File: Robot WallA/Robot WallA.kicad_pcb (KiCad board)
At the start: 4 copper layers, 170 x 100 mm, 316 parts, among them IC1 STM32F407IGT6, IC2 DS04-254-2-04BK-SMT, IC3 USBLC6-4SC6, IC4 USBLC6-4SC6, IC6 TLV75533PDBVR, IC7 ABXS005A4X341-SRZ, IC8 DRV8262DDVR, IC9 74LVC2G241DP-Q100H, J1 Conn_02x05_Female, J10 Conn_01x02, J11 Conn_01x02, J12 Conn_01x02, J13 10129383-916001ALF, J15 39501-1002, J16 39501-1002, J17 39501-1004, J18 39501-1004, J19 22-03-5035, J2 USB4216-03-A, J20 22-03-5035, J21 22-03-5035, J22 22-03-5035, J23 Conn_01x03, J24 281695-3, J25 Conn_01x03, J26 281695-3, J27 Conn_01x03, J28 281695-3, J29 Conn_01x03, J3 SS-90000-009, J30 39501-1002, J31 39501-1002, J32 Conn_01x03, J33 281695-3, J34 Conn_01x03, J35 SM04B-SRSS-TB, J36 SM04B-SRSS-TB, J37 SM04B-SRSS-TB, J38 SM02B-SRSS-TB_LF__SN_, J39 Conn_01x03, J4 USB_B_Micro, J40 SM03B-SRSS-TB_LF__SN_, J41 SM03B-SRSS-TB_LF__SN_, J42 SM03B-SRSS-TB_LF__SN_, J43 SM03B-SRSS-TB_LF__SN_, J44 SM02B-SRSS-TB_LF__SN_, J45 SM04B-SRSS-TB, J46 SM02B-SRSS-TB_LF__SN_, J47 SM02B-SRSS-TB_LF__SN_, J6 10129383-916001ALF, J7 Conn_01x02, J8 XT90PW_M, J9 Conn_01x02, Q1 BSS138, Q2 BSS138, Q3 BSS138, Q4 BSS119, Q5 BSS119, Q6 BSS138, SW1 Switch, T1 H1102NL, U1 FT231XS, U10 PTN78060W_EUW-7, U2 125700D00000G, U3 125700D00000G, U4 125700D00000G, U5 125700D00000G, U6 L298N, U7 LAN8742A, U8 PTN78020W, U9 PTN78060W_EUW-7, Y1 Crystal_GND24, Y2 Crystal_GND24

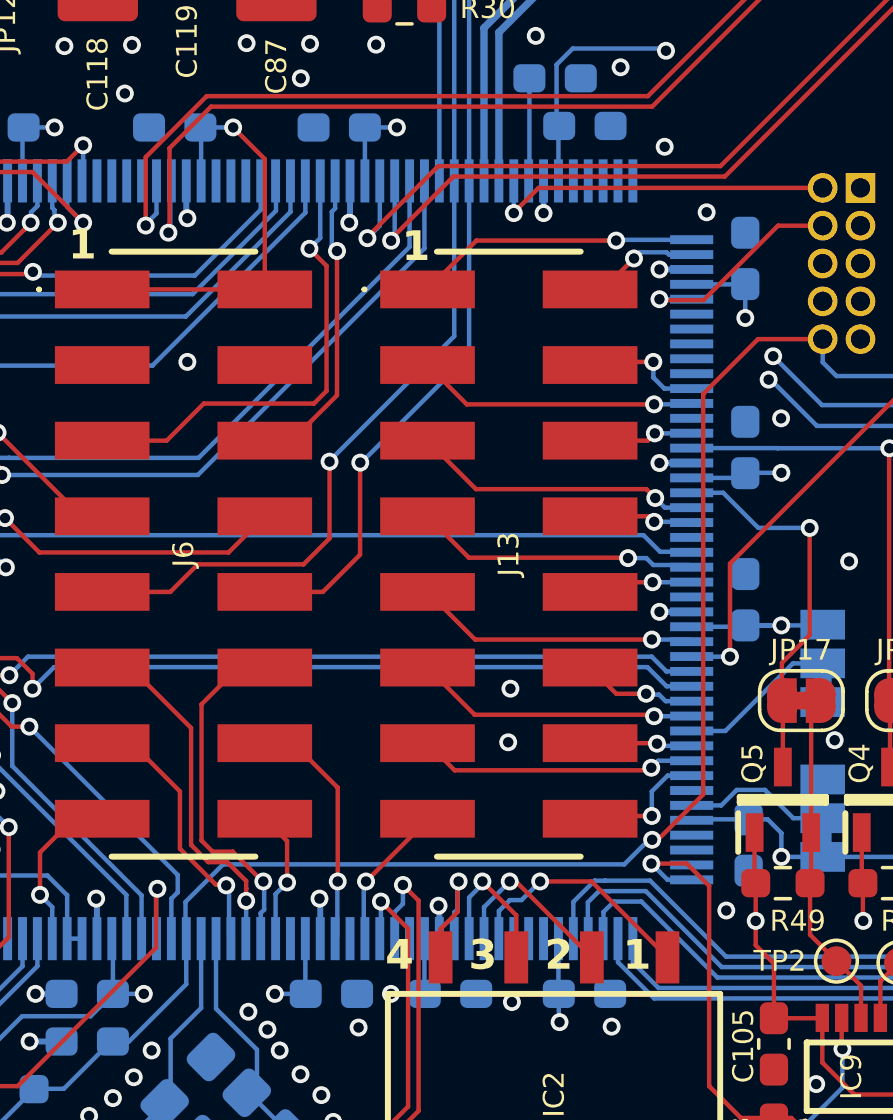
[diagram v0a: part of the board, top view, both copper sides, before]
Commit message: Modified a bit pin header pins to allow I2C,SPI and CAN
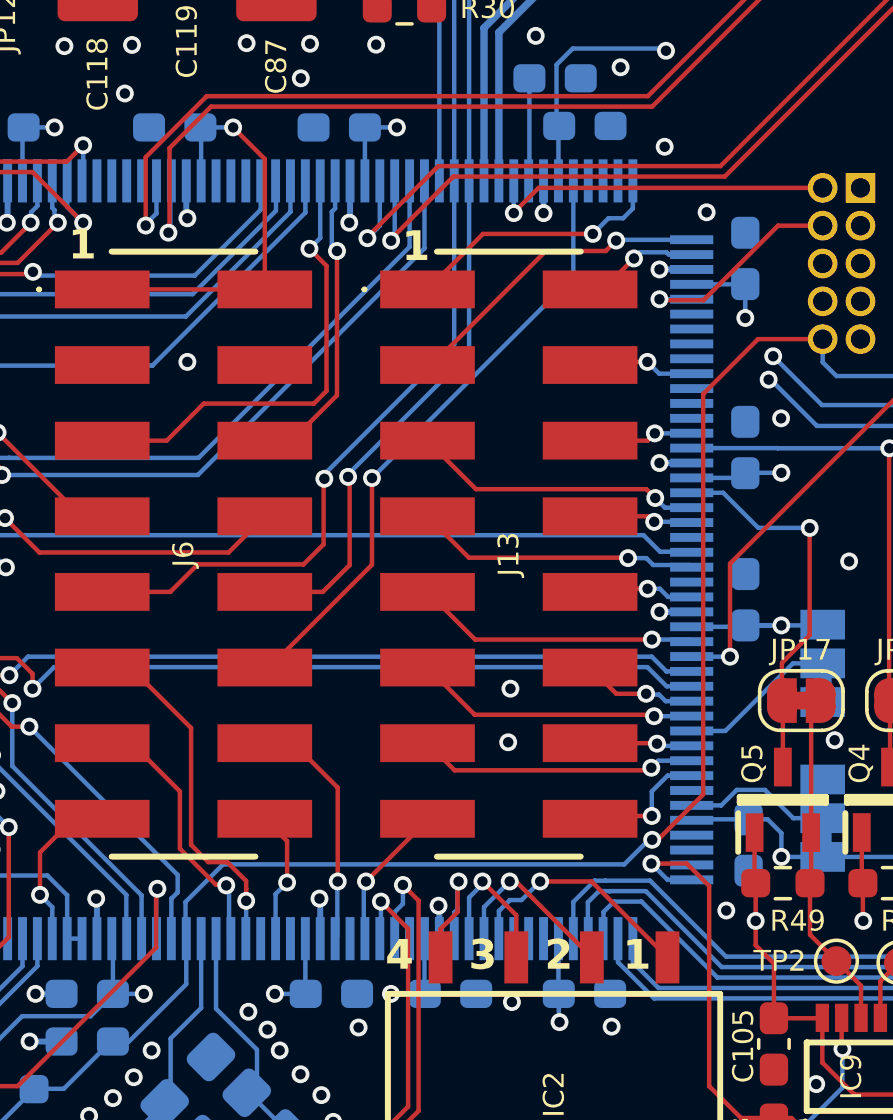
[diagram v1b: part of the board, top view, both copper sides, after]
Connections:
- IC1 pad 128: unconnected-(IC1-PH13-Pad128) -> /MCU/MCU_Core/PH13
- IC1 pad 132: unconnected-(IC1-PI1-Pad132) -> /MCU/MCU_Core/PI1
- IC1 pad 142: unconnected-(IC1-PD0-Pad142) -> /MCU/MCU_Core/PD0
- IC1 pad 143: /MCU/MCU_Core/PD1 -> unconnected-(IC1-PD1-Pad143)
- IC1 pad 144: /MCU/MCU_Core/PD2 -> unconnected-(IC1-PD2-Pad144)
- IC1 pad 156: /MCU/MCU_Core/PG13 -> unconnected-(IC1-PG13-Pad156)
- IC1 pad 157: unconnected-(IC1-PG14-Pad157) -> /MCU/MCU_Core/PG14
- IC1 pad 26: /MCU/MCU_Core/PF8 -> unconnected-(IC1-PF8-Pad26)
- J13 pad A1: /MCU/MCU_Core/PI2 -> /MCU/MCU_Core/PI1
- J13 pad A2: /MCU/MCU_Core/PD2 -> /MCU/MCU_Core/PI2
- J13 pad B2: /MCU/MCU_Core/PD1 -> /MCU/MCU_Core/PD0
- J13 pad B5: /MCU/MCU_Core/PG13 -> /MCU/MCU_Core/PG14
- J6 pad B6: /MCU/MCU_Core/PF8 -> /MCU/MCU_Core/PH13
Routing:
- net /MCU/MCU_Core/PH13: track 0.00 -> 20.7 mm, vias 0 -> 1
- net /MCU/MCU_Core/PF8: track 10.9 -> 0.00 mm, vias 1 -> 0
- net /MCU/MCU_Core/PD2: track 9.39 -> 0.00 mm, vias 1 -> 0
- net /MCU/MCU_Core/PI1: track 0.00 -> 8.95 mm, vias 0 -> 1
- net /MCU/MCU_Core/PD1: track 3.99 -> 0.00 mm, vias 1 -> 0
- net /MCU/MCU_Core/PG14: track 0.00 -> 3.57 mm, vias 0 -> 1
- net /MCU/MCU_Core/PD0: track 0.00 -> 3.47 mm, vias 0 -> 1
- net /MCU/MCU_Core/PG13: track 3.08 -> 0.00 mm, vias 1 -> 0
- net /MCU/MCU_Core/PI2: track 9.56 -> 10.6 mm

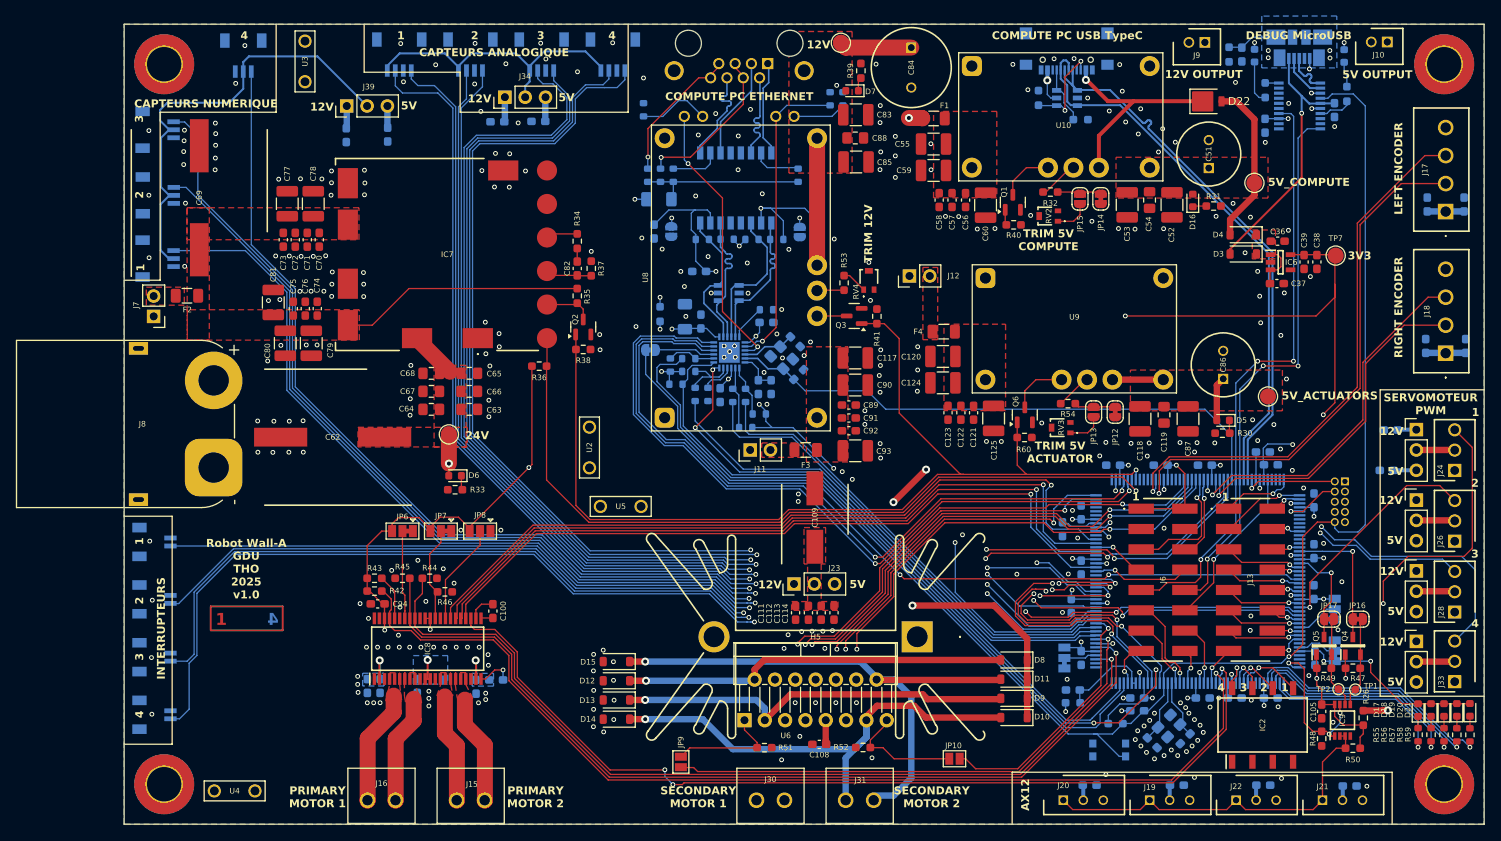
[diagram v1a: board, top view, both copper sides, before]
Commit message: Added pin header for 5V USB type output, to be able to disable it
Updated fab files
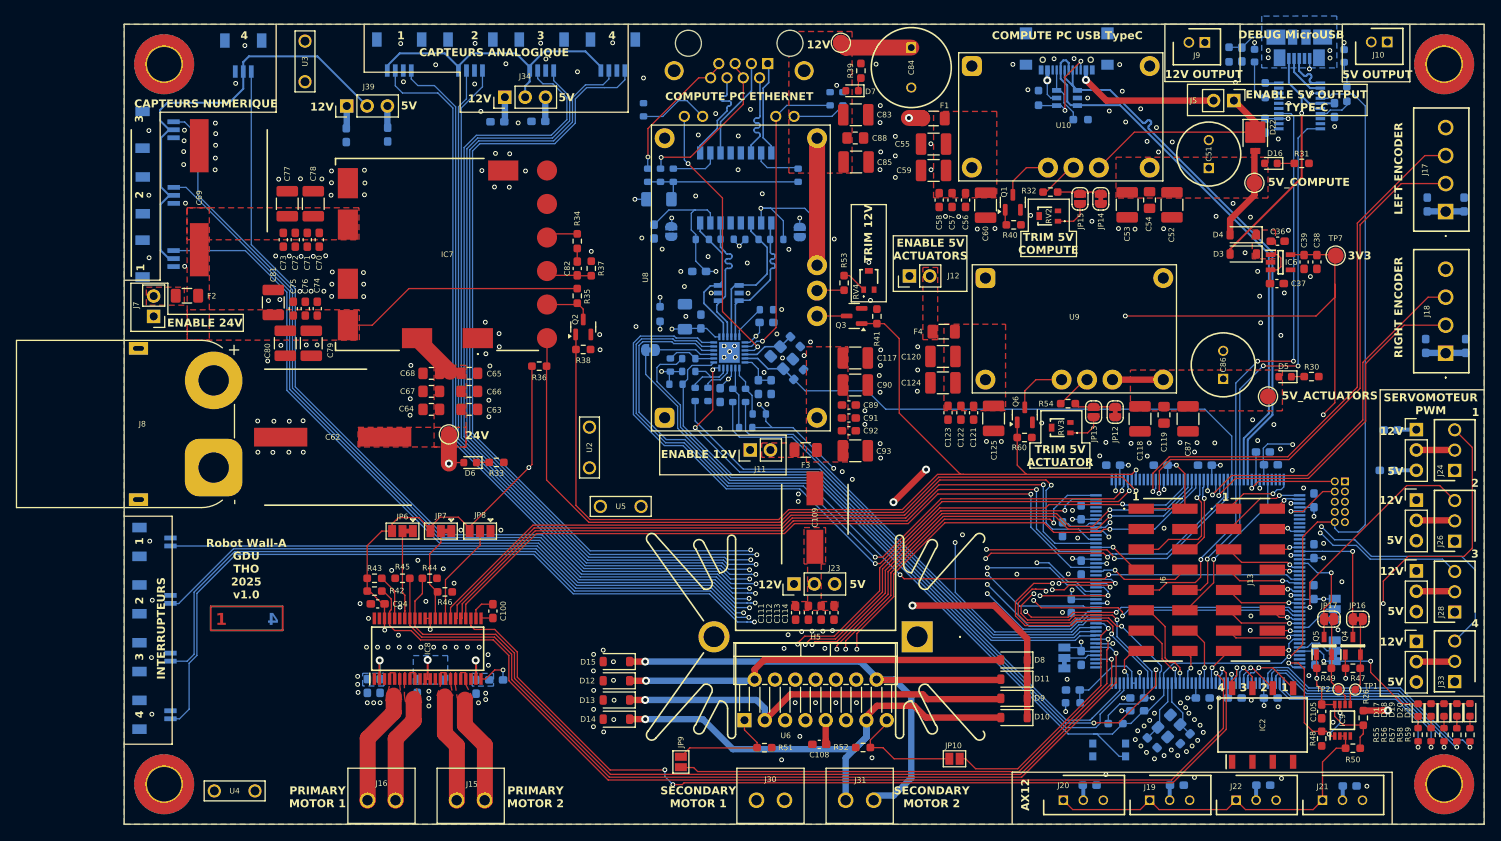
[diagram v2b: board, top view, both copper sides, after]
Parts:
- added J5: Conn_01x02, Connector_PinHeader_2.54mm:PinHeader_1x02_P2.54mm_Vertical, F.Cu at (193.9, 49.0)
- moved R30 13.2 mm to (203.6, 83.5), turned to 0 degrees
- moved R31 12.2 mm to (202.4, 56.9)
- moved D16 10.8 mm to (198.6, 56.9), turned to 180 degrees
- moved D5 9.47 mm to (200.3, 83.5)
- moved D22 7.43 mm to (196.6, 53.7), turned to -90 degrees
- moved R33 6.20 mm to (101.8, 94.2), turned to 0 degrees
- moved D6 2.49 mm to (98.5, 94.3)
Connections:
- D22 pad 1: /MCU/MCU_Peripherals/5V_USB -> /Power/Power_Buck_5V_Compute/5V_sense
- U10 pad 5: /MCU/MCU_Peripherals/5V_USB -> /Power/Power_Buck_5V_Compute/5V_sense
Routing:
- net /Power/Power_Buck_5V_Compute/5V_sense: track 0.00 -> 26.4 mm
- net /MCU/5V_PC_EMBARQUE: track 20.7 -> 11.8 mm
- net /MCU/MCU_Peripherals/5V_USB: track 36.3 -> 27.5 mm
- net /Motor/5V: track 407.3 -> 401.8 mm
- net Net-(D16-K): track 1.60 -> 2.15 mm
- net GND: vias 324 -> 323
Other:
- board text added: "ENABLE 12V"
- board text added: "ENABLE 24V"
- board text added: "ENABLE 5V ACTUATORS"
- board text added: "ENABLE 5V OUTPUT TYPE-C"

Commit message: Added 3 thermistor to measure temperature near 12V and 24V power supplies and near motor drivers
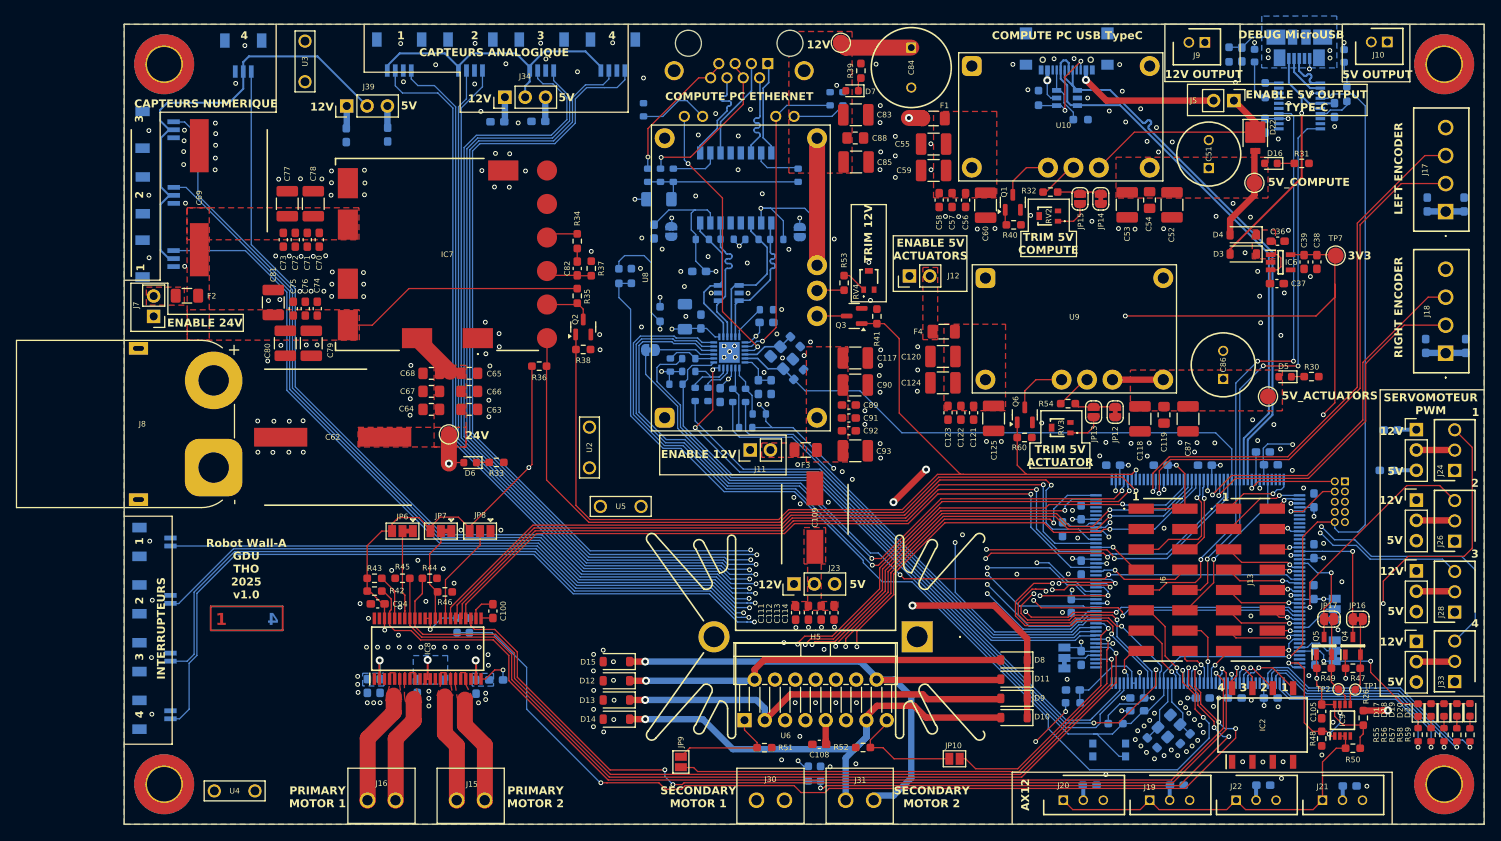
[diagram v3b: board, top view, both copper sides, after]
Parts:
- added R61: 10k, Resistor_SMD:R_0603_1608Metric_Pad0.98x0.95mm_HandSolder, B.Cu at (117.0, 71.0)
- added R62: 10k, Resistor_SMD:R_0603_1608Metric_Pad0.98x0.95mm_HandSolder, B.Cu at (96.8, 114.6)
- added R63: 10k, Resistor_SMD:R_0603_1608Metric_Pad0.98x0.95mm_HandSolder, B.Cu at (140.7, 133.2)
- added TH1: Thermistor_NTC, Resistor_SMD:R_0603_1608Metric_Pad0.98x0.95mm_HandSolder, B.Cu at (118.6, 70.9)
- added TH2: Thermistor_NTC, Resistor_SMD:R_0603_1608Metric_Pad0.98x0.95mm_HandSolder, B.Cu at (98.4, 114.6)
- added TH3: Thermistor_NTC, Resistor_SMD:R_0603_1608Metric_Pad0.98x0.95mm_HandSolder, B.Cu at (142.3, 133.2)
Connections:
- IC1 pad 20: unconnected-(IC1-PF4-Pad20) -> /MCU/MCU_Core/PF4
- IC1 pad 24: unconnected-(IC1-PF6-Pad24) -> /MCU/WHEEL8
- IC1 pad 25: /MCU/MCU_Core/PF7 -> /MCU/SECONDARY_MOTOR8
- IC1 pad 26: unconnected-(IC1-PF8-Pad26) -> /Power/Temperature
- J6 pad B7: /MCU/MCU_Core/PF5 -> /MCU/MCU_Core/PF4
- J6 pad B8: /MCU/MCU_Core/PF7 -> /MCU/MCU_Core/PF5
- J8 pad MP: (no net) -> GND
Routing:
- net /MCU/WHEEL8: track 0.00 -> 125.7 mm, vias 0 -> 4
- net /Power/Temperature: track 0.00 -> 123.4 mm, vias 0 -> 2
- net /MCU/SECONDARY_MOTOR8: track 0.00 -> 69.3 mm, vias 0 -> 4
- net /MCU/3V3: track 464.7 -> 519.7 mm, vias 28 -> 30
- net /MCU/MCU_Core/PF4: track 0.00 -> 8.95 mm, vias 0 -> 1
- net /MCU/MCU_Core/PF7: track 4.50 -> 0.00 mm, vias 1 -> 0
- net /MCU/MCU_Core/PF5: track 7.12 -> 5.74 mm
- net /MCU/MCU_Core/ETH7: track 70.3 -> 69.4 mm
- net GND: vias 323 -> 329
